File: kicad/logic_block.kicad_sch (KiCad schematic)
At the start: 51 parts, among them J201 PT 1,5/20-3,5-H, U201 MCP23S17T-E/SS, U202 TBD62083AFNG, U203 TBD62083AFNG

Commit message: feat: update resistor array footprint, change power trace thickness, optimize design
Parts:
- RN201, RN202, RN203, RN204: footprint Resistor_SMD:R_Array_Convex_8x0602 -> Project_Library:R_Array_Convex_8x0602_EXB2HV
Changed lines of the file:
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@@
 			)
 		)
-		(property "Footprint" "Resistor_SMD:R_Array_Convex_8x0602"
+		(property "Footprint" "Project_Library:R_Array_Convex_8x0602_EXB2HV"
 			(at 162.56 126.365 90)
 			(effects
@@
 			)
 		)
-		(property "Footprint" "Resistor_SMD:R_Array_Convex_8x0602"
+		(property "Footprint" "Project_Library:R_Array_Convex_8x0602_EXB2HV"
 			(at 160.655 128.27 90)
 			(effects
@@
 			)
 		)
-		(property "Footprint" "Resistor_SMD:R_Array_Convex_8x0602"
+		(property "Footprint" "Project_Library:R_Array_Convex_8x0602_EXB2HV"
 			(at 162.56 73.025 90)
 			(effects
@@
 			)
 		)
-		(property "Footprint" "Resistor_SMD:R_Array_Convex_8x0602"
+		(property "Footprint" "Project_Library:R_Array_Convex_8x0602_EXB2HV"
 			(at 160.655 74.93 90)
 			(effects

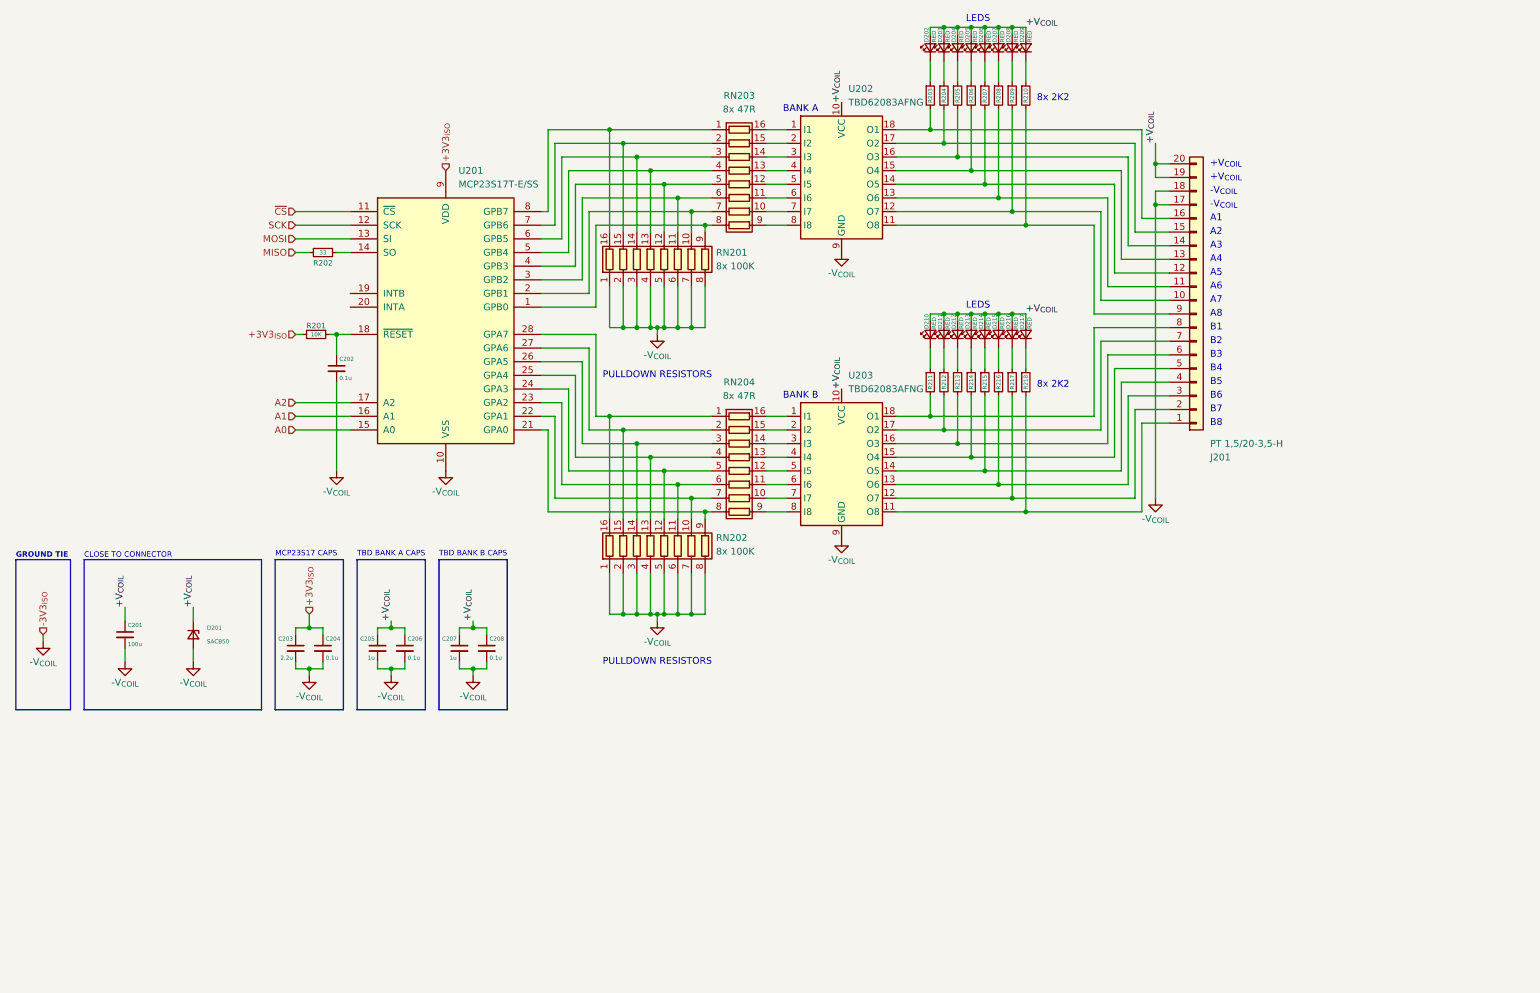
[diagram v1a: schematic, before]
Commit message: feat: add pluggable connector, add JLCPCB production files, improve routing
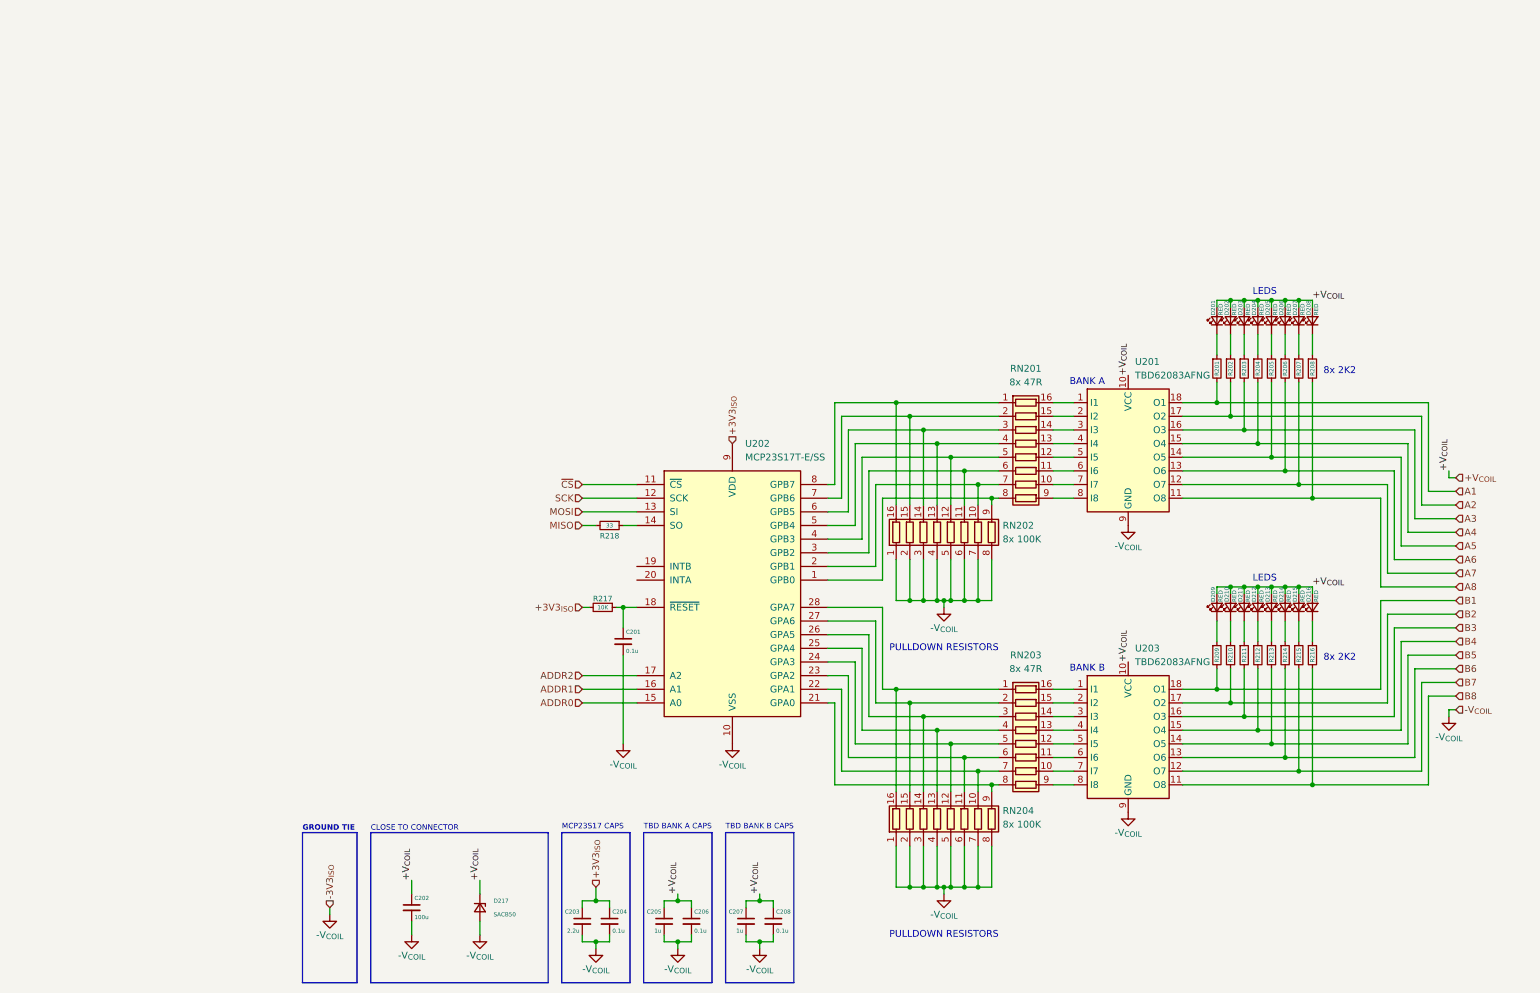
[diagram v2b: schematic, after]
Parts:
- removed J201: PT 1,5/20-3,5-H, Project_Library:TerminalBlock_Phoenix_PT-1,5-20-3.5-H_1x20_P3.50mm_Horizontal_No_SilkScreen, symbol Connector_Generic:Conn_01x20
- removed R201: 10K, Resistor_SMD:R_0603_1608Metric, symbol Device:R_Small
- removed R202: 33, Resistor_SMD:R_0603_1608Metric, symbol Device:R_Small
- added R217: 10K, Resistor_SMD:R_0603_1608Metric, symbol Device:R_Small
- added R218: 33, Resistor_SMD:R_0603_1608Metric, symbol Device:R_Small
- renumbered C202 to C201, C201 to C202, D202 to D201, D203 to D202, D204 to D203, D205 to D204, D206 to D205, D207 to D206, D208 to D207, D209 to D208, D210 to D209, D211 to D210, D212 to D211, D213 to D212, D214 to D213, D215 to D214, D216 to D215, D217 to D216, D201 to D217, R203 to R201, R204 to R202, R205 to R203, R206 to R204, R207 to R205, R208 to R206, R209 to R207, R210 to R208, R217 to R209, R218 to R210, RN203 to RN201, RN201 to RN202, RN204 to RN203, RN202 to RN204, U202 to U201, U201 to U202
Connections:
- net +3V3_{ISO}: now also R217.2
- net A1: now also R201.2, U201.18 (O1); no longer U202.16 (A1)
- net A2: now also R202.2, U201.17 (O2); no longer U202.17 (A2)
- net MISO: now also R218.2
- net A6: now reaches R206.2, U201.13 (O6)
- net at D211.1 (K): now also R211.1; no longer R213.1
- net A8: now reaches R208.2, U201.11 (O8)
- net at R216.1: now also D216.1 (K); no longer D214.1 (K)
- net B6: now reaches U203.13 (O6)
- net B6: now also R214.2; no longer R216.2
- net B3: now reaches U203.16 (O3)
- net B3: now also R211.2; no longer R213.2
- net at R210.1: now also D210.1 (K); no longer D216.1 (K)
- net at C201.1, U202.18 (~{RESET}): now also R217.1
- net at R212.1: now also D212.1 (K); no longer D210.1 (K)
- net B2: now reaches R210.2
- net B2: now also U203.17 (O2); no longer U203.11 (O8)
- net B1: now reaches R209.2
- net B1: now also U203.18 (O1); no longer U203.12 (O7)
- net B5: now reaches U203.14 (O5)
- net B5: now also R213.2; no longer R215.2
- net B4: now reaches U203.15 (O4)
- net B4: now also R212.2; no longer R214.2
- net at R214.1: now also D214.1 (K); no longer D212.1 (K)
- net at D209.1 (K): now also R209.1; no longer R211.1
- net A4: now reaches R204.2, U201.15 (O4)
- net A7: now reaches R207.2, U201.12 (O7)
- net at U202.14 (SO): now also R218.1
- net at D215.1 (K): now also R215.1; no longer R209.1
- net A3: now reaches R203.2, U201.16 (O3)
- net A5: now reaches R205.2, U201.14 (O5)
- net at D213.1 (K): now also R213.1; no longer R215.1
- net A0 renamed ADDR0
- new net ADDR1: U202.16 (A1)
- new net ADDR2: U202.17 (A2)
- new net B7: R215.2, U203.12 (O7)
- new net B8: R216.2, U203.11 (O8)
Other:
- note removed: "+V_{COIL}"
- note removed: "-V_{COIL}"
- note removed: "A1"
- note removed: "A2"
- note removed: "A3"
- note removed: "A4"
- note removed: "A5"
- note removed: "A6"
- note removed: "A7"
- note removed: "A8"
- note removed: "B1"
- note removed: "B2"
- note removed: "B3"
- note removed: "B4"
- note removed: "B5"
- note removed: "B6"
- note removed: "B7"
- note removed: "B8"
- moved on the sheet: C201, C202, C203, C204, C205, C206, C207, C208, D201, D202, D203, D204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

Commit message: feat: add extra power rail protection
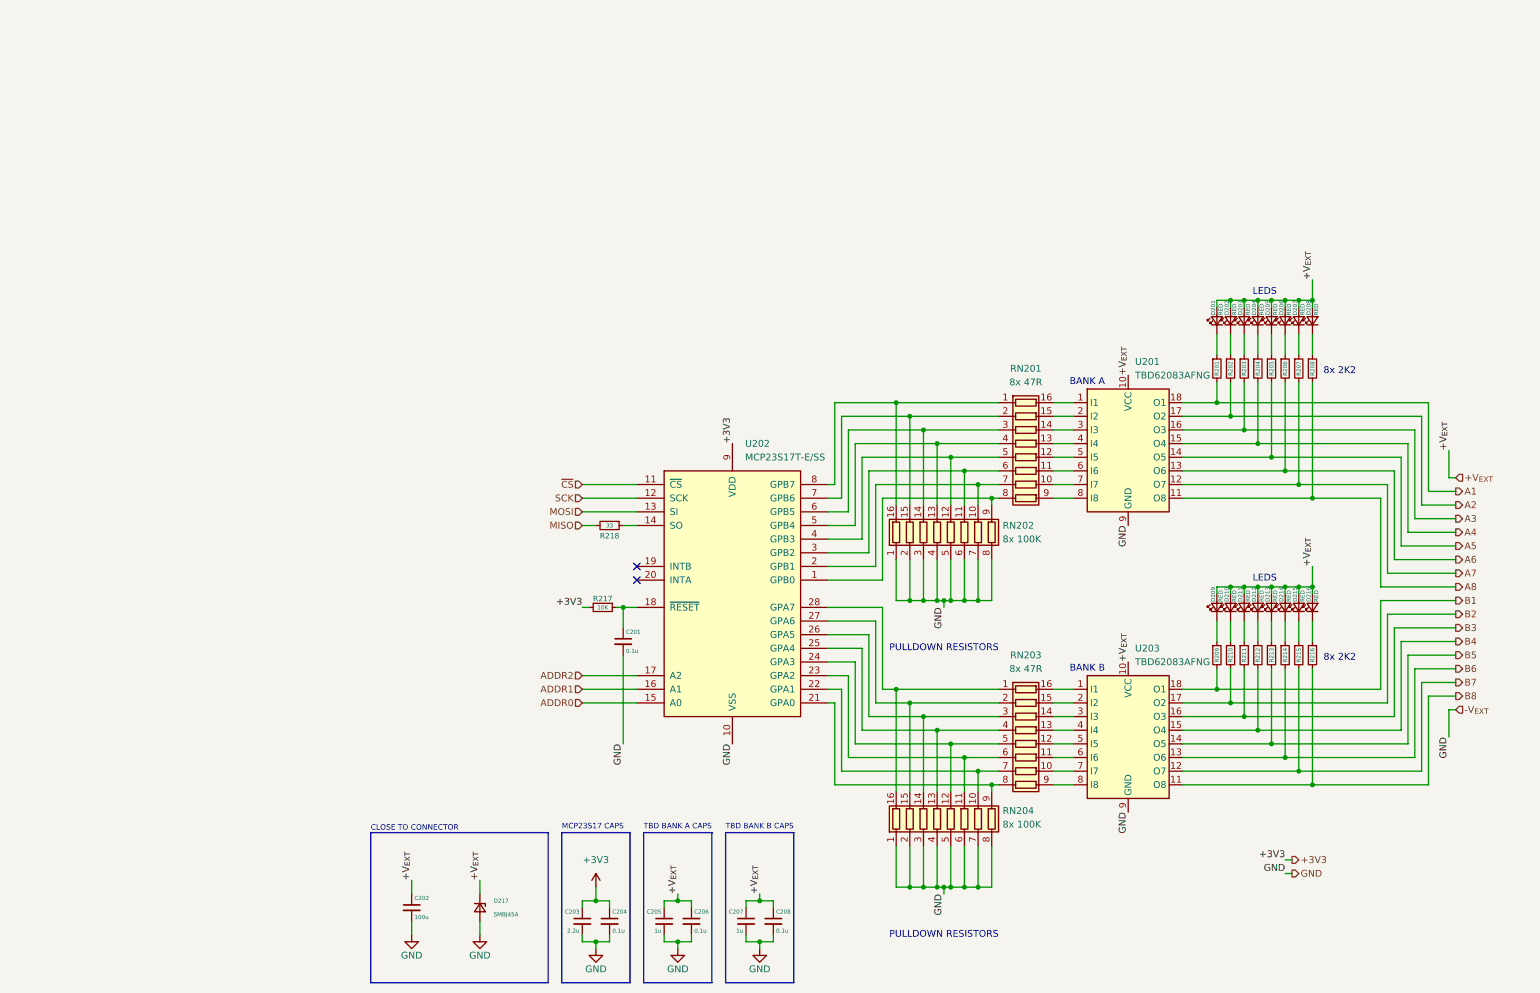
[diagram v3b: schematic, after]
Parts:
- D217: value SACB50 -> SMBJ45A; Mouser Part Number 576-SACB50 -> 576-SMBJ45A; Part Number SACB50 -> SMBJ45A
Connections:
- net +3V3_{ISO} renamed +3V3
- net +V_{COIL} renamed +V_{EXT}
- net -V_{COIL} renamed GND
- no-connect marks 0 -> 2
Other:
- note removed: "GROUND TIE"
